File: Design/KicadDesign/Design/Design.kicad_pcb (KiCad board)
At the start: 2 copper layers, 117.2 x 47.5 mm, 16 parts, among them J1 Screw_Terminal_01x02, J2 Screw_Terminal_01x02, Q1 IRF740, U1 IR2110, U2 TL494, U4 LM7809CT

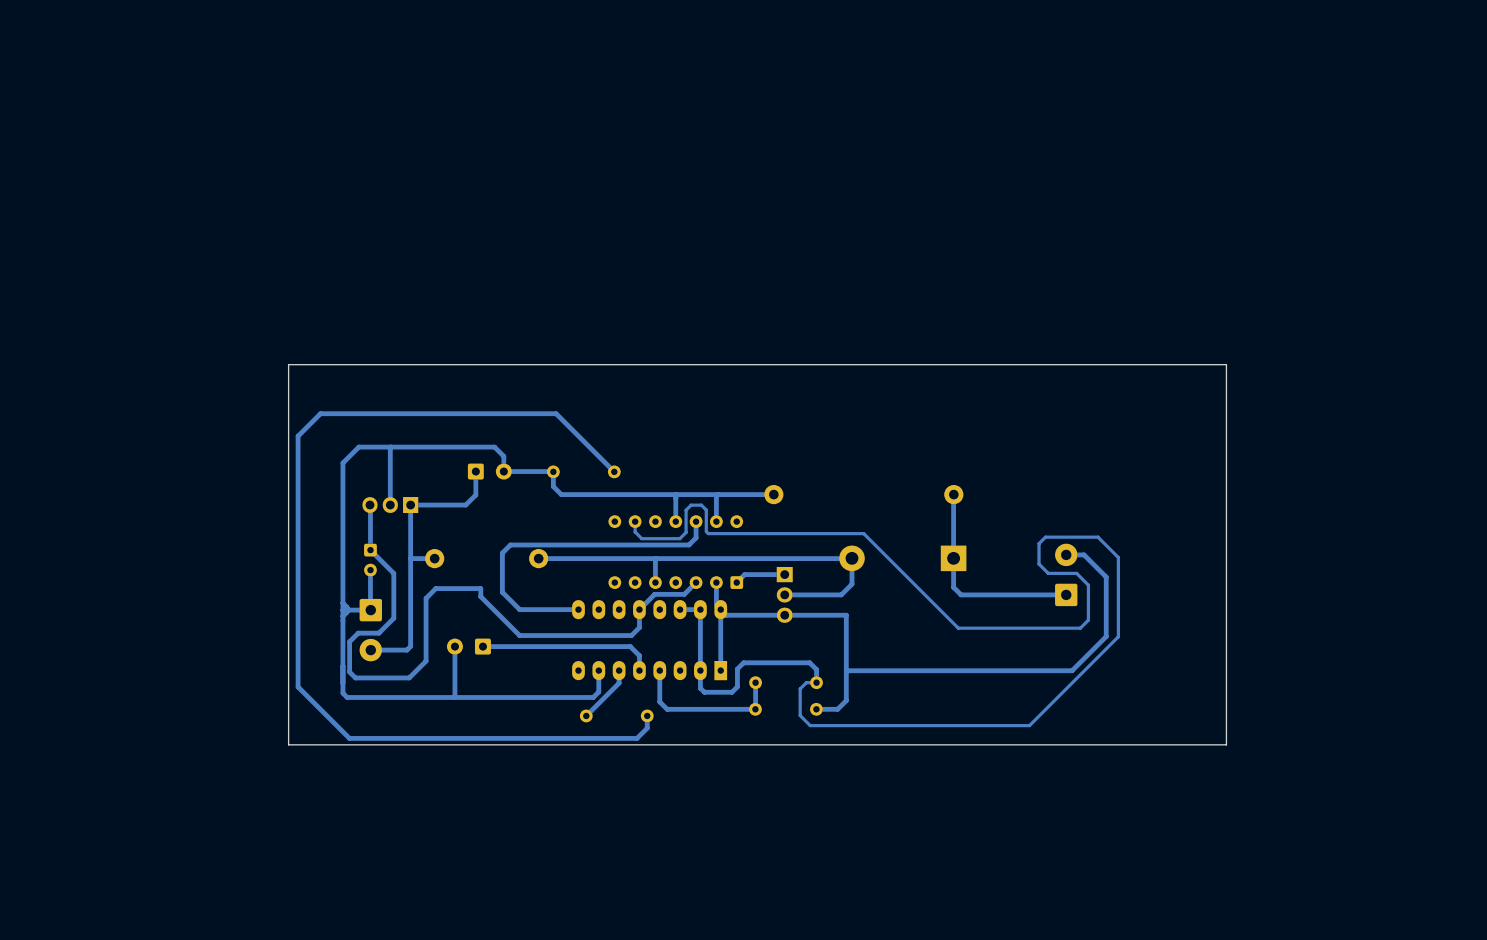
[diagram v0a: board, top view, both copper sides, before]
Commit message: Added LC Filter
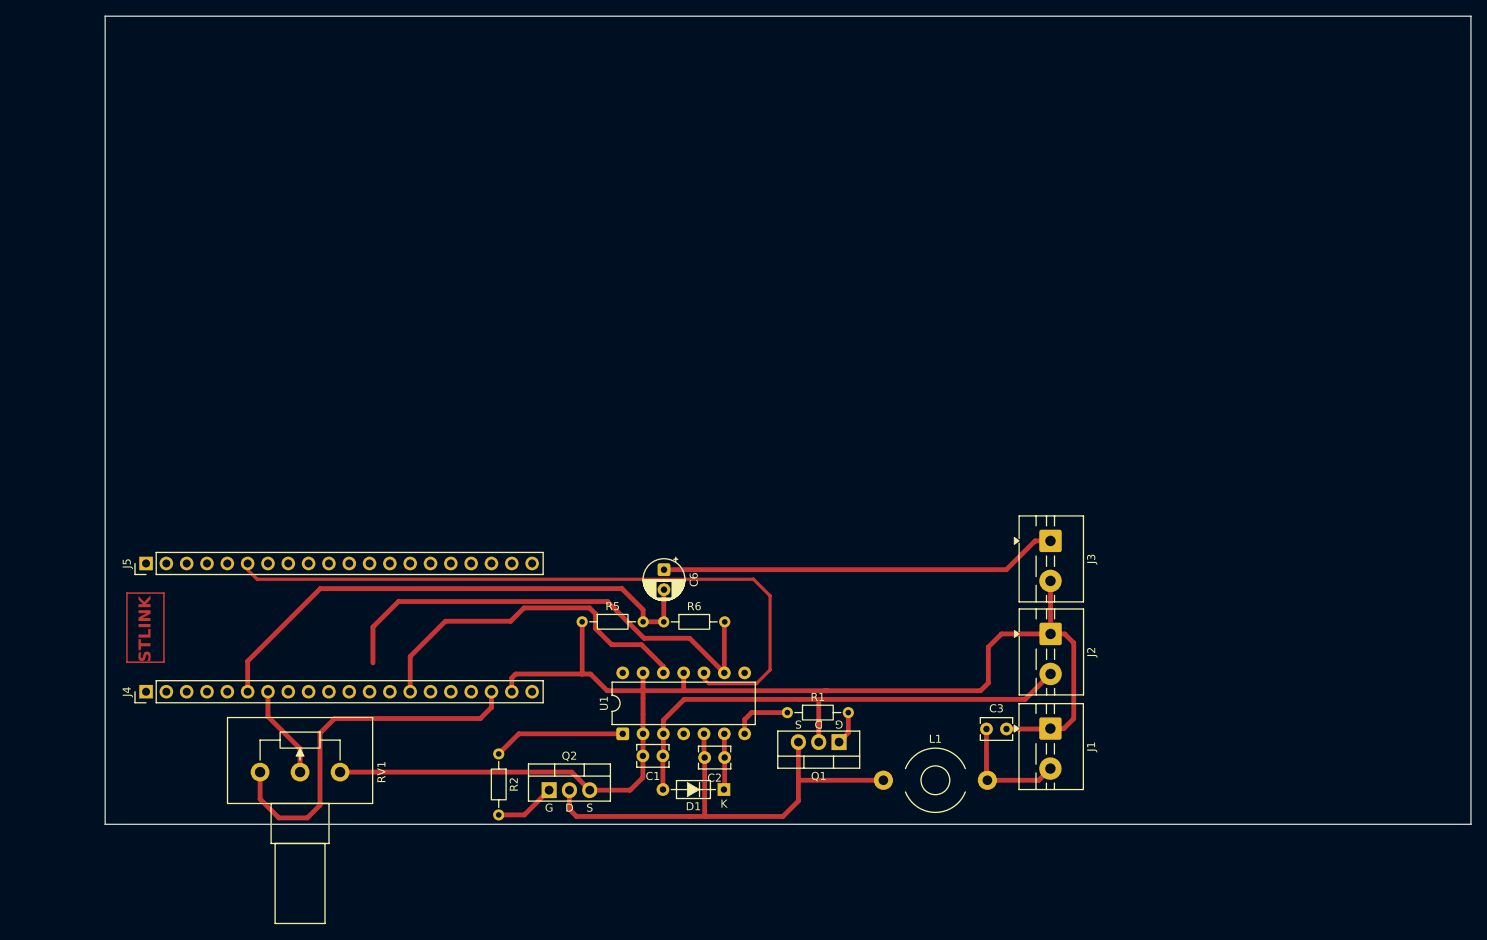
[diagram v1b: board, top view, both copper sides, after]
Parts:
- removed C4: 0.1u, Capacitor_THT:CP_Radial_D5.0mm_P2.50mm
- removed R3, R4: R_0201, Resistor_THT:R_Axial_DIN0207_L6.3mm_D2.5mm_P7.62mm_Horizontal
- removed U2: TL494, PCM_Package_DIP_AKL:DIP-16_W7.62mm_Socket_LongPads
- removed U4: LM7809CT, PCM_Package_TO_SOT_THT_AKL:TO-220-3_Vertical
- added C6: 4.7u, Capacitor_THT:CP_Radial_D5.0mm_P2.50mm, F.Cu at (133.6, 87.9)
- added J3: Jack 3.5 mm, TerminalBlock:TerminalBlock_MaiXu_MX126-5.0-02P_1x02_P5.00mm, F.Cu at (181.9, 84.3)
- added J4: Conn_01x20_Socket, Connector_PinHeader_2.54mm:PinHeader_1x20_P2.54mm_Vertical, F.Cu at (68.9, 103.2)
- added J5: Conn_01x20_Socket, Connector_PinHeader_2.54mm:PinHeader_1x20_P2.54mm_Vertical, F.Cu at (68.9, 87.2)
- added Q2: IRLZ44N, PCM_Package_TO_SOT_THT_AKL:TO-220-3_Vertical_GDS, F.Cu at (119.2, 115.5)
- added R5: 10k, Resistor_THT:R_Axial_DIN0204_L3.6mm_D1.6mm_P7.62mm_Horizontal, F.Cu at (123.4, 94.4)
- added R6: 10k, Resistor_THT:R_Axial_DIN0204_L3.6mm_D1.6mm_P7.62mm_Horizontal, F.Cu at (133.6, 94.5)
- added RV1: 20K, PCM_Potentiometer_THT_AKL:Potentiometer_Alps_RK163_Single_Horizontal, F.Cu at (83.1, 113.2)
- C1: value C_Rect_L26.5mm_W8.5mm_P22.50mm -> 470n; footprint PCM_Capacitor_THT_AKL:C_Rect_L26.5mm_W8.5mm_P22.50mm_MKS4 -> Capacitor_THT:C_Disc_D3.8mm_W2.6mm_P2.50mm; moved to F.Cu
- C2: value 1nF -> 470n; footprint Capacitor_THT:CP_Radial_D10.0mm_P3.50mm -> Capacitor_THT:C_Disc_D3.8mm_W2.6mm_P2.50mm; moved to F.Cu
- C3: footprint Capacitor_THT:CP_Radial_D10.0mm_P3.50mm -> Capacitor_THT:C_Disc_D3.8mm_W2.6mm_P2.50mm; moved to F.Cu
- D1: value MUR460 -> 1N4148; footprint PCM_Diode_THT_AKL:D_DO-201AD_P12.70mm_Horizontal -> PCM_Diode_THT_AKL:D_DO-35_SOD27_P7.62mm_Horizontal; moved to F.Cu
- J1: value Screw_Terminal_01x02 -> Speaker; moved to F.Cu
- J2: value Screw_Terminal_01x02 -> SourceSupply; moved to F.Cu
- L1, U1: moved to F.Cu
- Q1: value IRF740 -> IRLZ44N; moved to F.Cu
- R1, R2: value R_0201 -> 22; footprint Resistor_THT:R_Axial_DIN0207_L6.3mm_D2.5mm_P7.62mm_Horizontal -> Resistor_THT:R_Axial_DIN0204_L3.6mm_D1.6mm_P7.62mm_Horizontal; moved to F.Cu
- moved J2 85.0 mm to (181.9, 96.0)
- moved C3 71.5 mm to (173.9, 107.8)
- moved L1 62.6 mm to (161.0, 114.2)
- moved C1 48.9 mm to (133.5, 111.2)
- moved D1 40.7 mm to (141.1, 115.4)
- moved R2 35.9 mm to (112.9, 111.0), turned to -90 degrees
- moved C2 33.2 mm to (141.2, 111.4)
- moved U1 23.7 mm to (128.4, 108.4)
- moved Q1 22.0 mm to (155.5, 109.5), turned to 180 degrees
- moved R1 17.5 mm to (149.0, 105.8), turned to 0 degrees
- moved J1 16.8 mm to (181.9, 107.8), turned to -90 degrees
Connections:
- C1 pad 1: Net-(D1-K) -> 12V
- C2 pad 1: Net-(U2-CT) -> VB
- C2 pad 2: GND -> Net-(Q1-S)
- C3 pad 1: 24V -> Net-(J1-Pin_2)
- D1 pad 1: Net-(D1-K) -> VB
- D1 pad 2: D -> 12V
- J1 pad 1: Net-(D1-K) -> GND
- J1 pad 2: GND -> Net-(J1-Pin_2)
- J2 pad 2: 24V -> 12V
- L1 pad 1: 24V -> Net-(Q1-S)
- L1 pad 2: D -> Net-(J1-Pin_2)
- Q1 pad 2: D -> 12V
- Q1 pad 3: GND -> Net-(Q1-S)
- R1 pad 1: Net-(R1-Pad1) -> Net-(U1-HO)
- R1 pad 2: Net-(U2-RT) -> Net-(Q1-G)
- R2 pad 1: GND -> Net-(U1-LO)
- R2 pad 2: Net-(R1-Pad1) -> Net-(Q2-G)
- U1 pad 1: Net-(Q1-G) -> Net-(U1-LO)
- U1 pad 10: unconnected-(U1-HIN-Pad10) -> A9 PWM
- U1 pad 12: PWMOUT -> B0 PWM_N
- U1 pad 3: 9V -> 12V
- U1 pad 5: D -> Net-(Q1-S)
- U1 pad 6: unconnected-(U1-VB-Pad6) -> VB
- U1 pad 7: unconnected-(U1-HO-Pad7) -> Net-(U1-HO)
- U1 pad 9: REF -> 3.3V
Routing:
- net REF: track 187.9 -> 0.00 mm
- net Net-(R1-Pad1): track 123.8 -> 0.00 mm
- net 3.3V: track 0.00 -> 106.1 mm
- net A9 PWM: track 0.00 -> 86.7 mm
- net 9V: track 85.8 -> 0.00 mm
- net GND: track 248.2 -> 166.1 mm
- net A0 ADC1: track 0.00 -> 66.3 mm
- net 12V: track 0.00 -> 64.9 mm
- net Net-(Q1-S): track 0.00 -> 60.6 mm
- net D: track 54.4 -> 0.00 mm
- net Net-(J3-Pin_1): track 0.00 -> 49.8 mm
- net B0 PWM_N: track 0.00 -> 43.9 mm
- net PWMOUT: track 42.3 -> 0.00 mm
- net 24V: track 37.5 -> 0.00 mm
- net Net-(D1-K): track 26.1 -> 0.00 mm
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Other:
- board size 117.2 x 47.5 mm -> 170.7 x 101 mm
- board text added: "STLINK"

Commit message: Autorouted TODO: Check Autoroute traces
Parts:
- C1, C2, C3, C6, D1, J1, J2, J3, J4, J5, L1, Q1, Q2, R1, R2, R5, R6, RV1, U1: moved to B.Cu
- moved J2 121.4 mm to (60.5, 96.0)
- moved J3 121.4 mm to (60.5, 84.3)
- moved J1 121.4 mm to (60.5, 107.8)
- moved C3 105.4 mm to (68.5, 107.8), turned to 180 degrees
- moved L1 79.7 mm to (81.4, 114.2), turned to 180 degrees
- moved RV1 76.2 mm to (159.3, 113.2)
- moved Q1 68.6 mm to (86.9, 109.5), turned to 0 degrees
- moved J4 59.4 mm to (125.3, 84.6), turned to -90 degrees
- moved J5 58.0 mm to (125.3, 100.6), turned to -90 degrees
- moved R1 55.6 mm to (93.4, 105.8), turned to 180 degrees
- moved C2 40.0 mm to (101.2, 111.4), turned to 0 degrees
- moved D1 39.8 mm to (101.3, 115.4), turned to 0 degrees
- moved C6 24.8 mm to (108.8, 87.9)
- moved R6 24.7 mm to (108.8, 94.5), turned to 180 degrees
- moved C1 24.5 mm to (108.9, 111.2), turned to 0 degrees
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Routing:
- net A1 ADC2: track 11.7 -> 82.8 mm
- net A9 PWM: track 86.7 -> 36.0 mm
- net GND: track 166.1 -> 213.7 mm
- net 12V: track 64.9 -> 96.3 mm
- net A0 ADC1: track 66.3 -> 37.3 mm
- net B0 PWM_N: track 43.9 -> 56.1 mm
- net 3.3V: track 106.1 -> 109.4 mm
- net Net-(Q1-S): track 60.6 -> 62.4 mm
- net Net-(U1-HO): track 7.52 -> 6.44 mm

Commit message: Minor fixes on traces
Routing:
- net GND: track 213.7 -> 233.3 mm
- net A1 ADC2: track 82.8 -> 96.9 mm
- net Net-(Q1-S): track 62.4 -> 74.6 mm
- net 12V: track 96.3 -> 107.6 mm
- net 3.3V: track 109.4 -> 116.1 mm
- net B0 PWM_N: track 56.1 -> 59.7 mm
- net A9 PWM: track 36.0 -> 38.7 mm
- net A0 ADC1: track 37.3 -> 38.9 mm

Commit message: Minor fixes on traces
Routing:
- net GND: track 233.3 -> 237.5 mm
- net 12V: track 107.6 -> 109.0 mm
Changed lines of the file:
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@@
+	)
+	(segment
+		(start 96.82 100.99)
+		(end 96.82 102.45)
+		(width 0.6)
+		(layer "B.Cu")
+		(net 1)
 	)
 	(segment
@@
 	)
 	(segment
+		(start 96.82 99.4)
+		(end 96.82 94.68)
+		(width 0.6)
+		(layer "B.Cu")
+		(net 1)
+	)
+	(segment
 		(start 156.94 115.04)
 		(end 158.18 116.28)
@@
 	)
 	(segment
+		(start 63.58 107.79)
+		(end 63.87 107.79)
+		(width 0.6)
+		(layer "B.Cu")
+		(net 1)
+	)
+	(segment
 		(start 112.3383 111.2)
 		(end 111.4375 111.2)
@@
 	)
 	(segment
+		(start 63.58 107.2)
+		(end 64.17 107.79)
+		(width 0.6)
+		(layer "B.Cu")
+		(net 1)
+	)
+	(segment
 		(start 149.2875 113.23)
 		(end 149.2875 111.6225)
@@
 	)
 	(segment
+		(start 96.07 100.24)
+		(end 96.82 100.99)
+		(width 0.6)
+		(layer "B.Cu")
+		(net 1)
+	)
+	(segment
+		(start 64.17 107.79)
+		(end 65.9375 107.79)
+		(width 0.6)
+		(layer "B.Cu")
+		(net 1)
+	)
+	(segment
 		(start 111.4375 111.2)
 		(end 111.4175 111.18)
@@
 	)
 	(segment
+		(start 63.58 107.09)
+		(end 63.58 107.79)
+		(width 0.6)
+		(layer "B.Cu")
+		(net 1)
+	)
+	(segment
 		(start 96.82 94.68)
 		(end 99.31 92.19)
@@
 	)
 	(segment
+		(start 95.9 100.15)
+		(end 96.07 100.15)
+		(width 0.6)
+		(layer "B.Cu")
+		(net 1)
+	)
+	(segment
+		(start 96.07 100.15)
+		(end 96.07 100.24)
+		(width 0.6)
+		(layer "B.Cu")
+		(net 1)
+	)
+	(segment
 		(start 100.09 105.72)
 		(end 96.82 102.45)
@@
 	)
 	(segment
+		(start 95.9 100.15)
+		(end 96.69 100.15)
+		(width 0.6)
+		(layer "B.Cu")
+		(net 1)
+	)
+	(segment
 		(start 99.31 92.19)
 		(end 102.8 92.19)
@@
 	)
 	(segment
+		(start 63.58 96.98)
+		(end 63.58 107.09)
+		(width 0.6)
+		(layer "B.Cu")
+		(net 1)
+	)
+	(segment
 		(start 60.475 95.96)
 		(end 62.56 95.96)
@@
 	)
 	(segment
+		(start 96.07 100.15)
+		(end 96.82 99.4)
+		(width 0.6)
+		(layer "B.Cu")
+		(net 1)
+	)
+	(segment
 		(start 96.82 100.28)
-		(end 96.82 102.45)
+		(end 96.82 100.99)
 		(width 0.6)
 		(layer "B.Cu")
@@
 	(segment
 		(start 62.3936 107.79)
-		(end 63.87 107.79)
+		(end 62.88 107.79)
 		(width 0.6)
 		(layer "B.Cu")
@@
 	(segment
 		(start 73.6775 100.15)
-		(end 96.69 100.15)
+		(end 95.9 100.15)
+		(width 0.6)
+		(layer "B.Cu")
+		(net 1)
+	)
+	(segment
+		(start 62.88 107.79)
+		(end 63.58 107.09)
 		(width 0.6)
 		(layer "B.Cu")
@@
 	)
 	(segment
-		(start 63.87 97.27)
-		(end 63.87 107.79)
+		(start 62.56 95.96)
+		(end 63.58 96.98)
 		(width 0.6)
 		(layer "B.Cu")
@@
 	)
 	(segment
+		(start 62.88 107.79)
+		(end 63.58 107.79)
+		(width 0.6)
+		(layer "B.Cu")
+		(net 1)
+	)
+	(segment
 		(start 118.0775 115.485)
 		(end 116.6233 115.485)
@@
 	(segment
 		(start 63.87 107.79)
-		(end 65.9375 107.79)
+		(end 64.17 107.79)
 		(width 0.6)
 		(layer "B.Cu")
@@
 	(segment
 		(start 96.82 102.45)
-		(end 96.82 94.68)
-		(width 0.6)
-		(layer "B.Cu")
-		(net 1)
-	)
-	(segment
-		(start 62.56 95.96)
-		(end 63.87 97.27)
+		(end 96.82 99.4)
 		(width 0.6)
 		(layer "B.Cu")
@@
 	)
 	(segment
+		(start 63.58 107.09)
+		(end 63.58 107.2)
+		(width 0.6)
+		(layer "B.Cu")
+		(net 1)
+	)
+	(segment
 		(start 158.18 116.28)
 		(end 165.8 116.28)
@@
 	(segment
 		(start 77.13 107.63)
-		(end 77.13 116.97)
+		(end 77.13 116.31)
 		(width 0.6)
 		(layer "B.Cu")
@@
 	)
 	(segment
+		(start 77.13 116.31)
+		(end 77.13 116.54)
+		(width 0.6)
+		(layer "B.Cu")
+		(net 3)
+	)
+	(segment
+		(start 60.29 116.97)
+		(end 76.7 116.97)
+		(width 0.6)
+		(layer "B.Cu")
+		(net 3)
+	)
+	(segment
+		(start 77.13 116.31)
+		(end 77.13 116.97)
+		(width 0.6)
+		(layer "B.Cu")
+		(net 3)
+	)
+	(segment
+		(start 77.13 116.54)
+		(end 76.7 116.97)
+		(width 0.6)
+		(layer "B.Cu")
+		(net 3)
+	)
+	(segment
 		(start 108.8775 111.15)
 		(end 108.8775 108.445)
@@
 	)
 	(segment
+		(start 77.13 116.54)
+		(end 77.56 116.97)
+		(width 0.6)
+		(layer "B.Cu")
+		(net 3)
+	)
+	(segment
 		(start 79.6 116.97)
 		(end 78.5941 116.97)
@@
 	)
 	(segment
-		(start 60.29 116.97)
+		(start 76.7 116.97)
 		(end 77.13 116.97)
+		(width 0.6)
+		(layer "B.Cu")
+		(net 3)
+	)
+	(segment
+		(start 77.13 116.97)
+		(end 77.56 116.97)
 		(width 0.6)
 		(layer "B.Cu")
@@
 	)
 	(segment
-		(start 77.13 116.97)
+		(start 77.56 116.97)
 		(end 78.5941 116.97)
 		(width 0.6)
